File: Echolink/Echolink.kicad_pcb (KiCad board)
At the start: 2 copper layers, 80 x 45 mm, 45 parts, among them J1 USB_B, J2 AUDIO_PC, J3 AUDIO_TRX, J4 MountHole, J5 CAT, J6 PTT_CW, J7 MountHole, J8 MountHole, J9 MountHole, K11 TIANBO-HJR-4102-L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

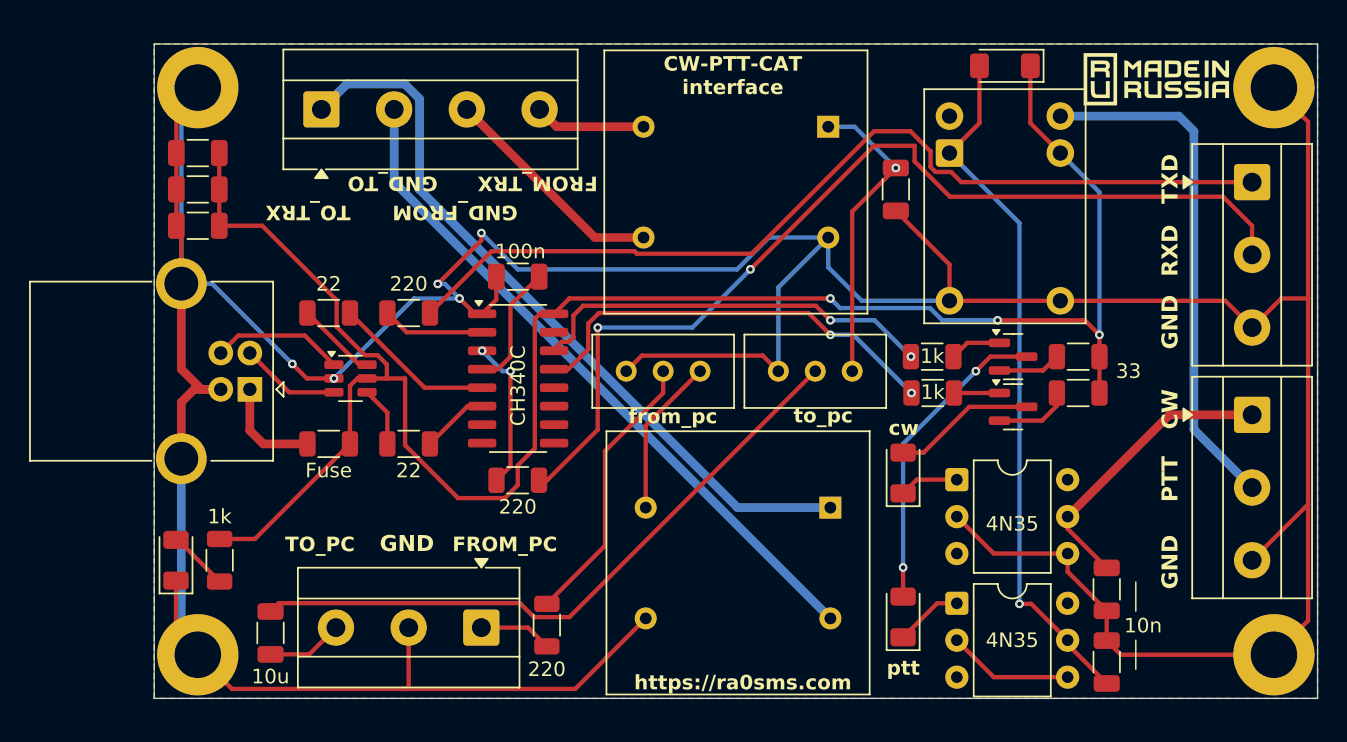
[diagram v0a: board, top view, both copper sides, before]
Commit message: change optotransistor, add some pics
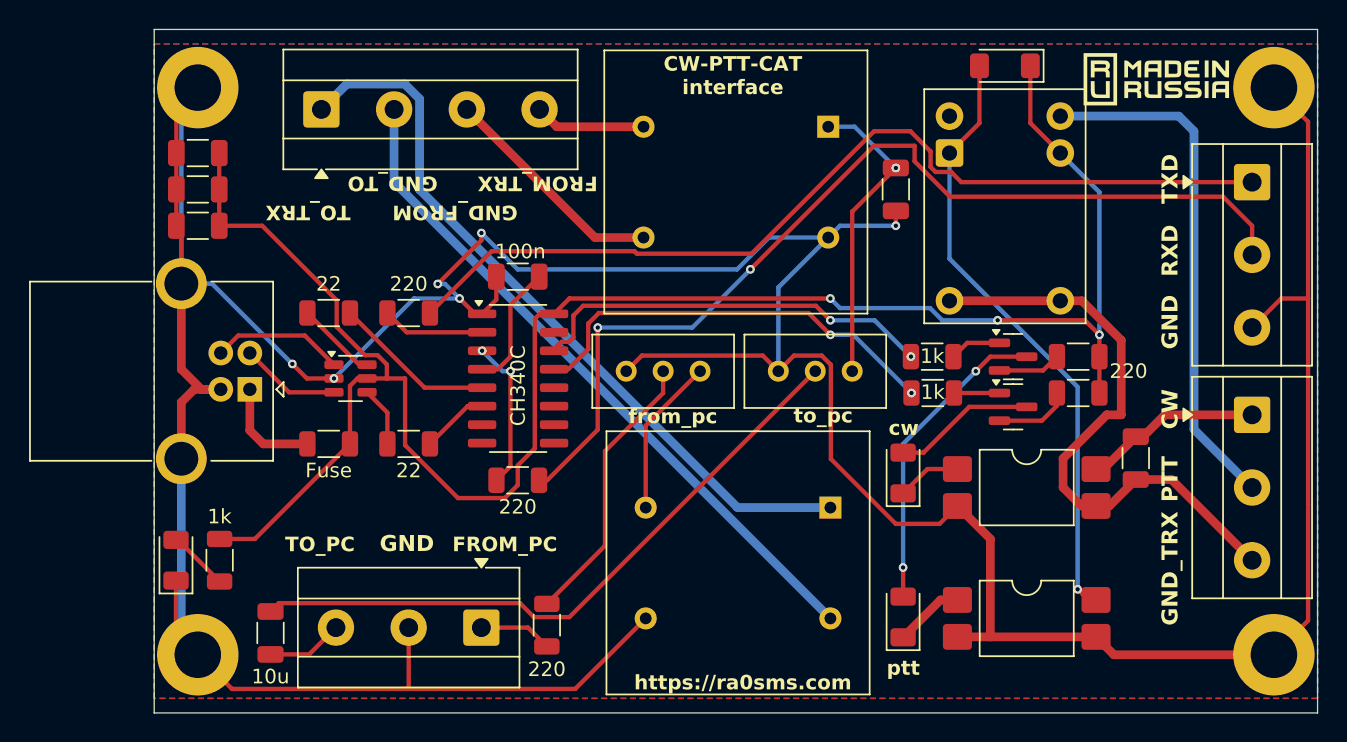
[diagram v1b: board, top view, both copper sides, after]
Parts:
- removed C6: 10n, Capacitor_SMD:C_1206_3216Metric
- removed U3, U4: 4N35, Package_DIP:DIP-6_W7.62mm
- added U5: LTV-817S, Package_DIP:SMDIP-4_W9.53mm, F.Cu at (192.0, 108.5)
- added U6: LTV-817S, Package_DIP:SMDIP-4_W9.53mm, F.Cu at (192.0, 99.5)
- R7: value 33 -> 220
- moved C5 9.24 mm to (199.5, 97.5)
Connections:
- C5 pad 2: GND -> GNDREF
- J6 pad 3: GND -> GNDREF
- K11 pad 11: GND -> GNDREF
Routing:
- net GNDREF: track 0.00 -> 41.9 mm
- net GND: track 314.7 -> 292.3 mm, vias 5 -> 6
- net CW: track 20.2 -> 12.3 mm
- net Net-(D3-A): track 48.3 -> 42.1 mm
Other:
- board size 80 x 45 mm -> 80 x 47 mm
- board text added: "GND_TRX"
